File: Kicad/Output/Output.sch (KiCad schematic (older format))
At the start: 4 parts

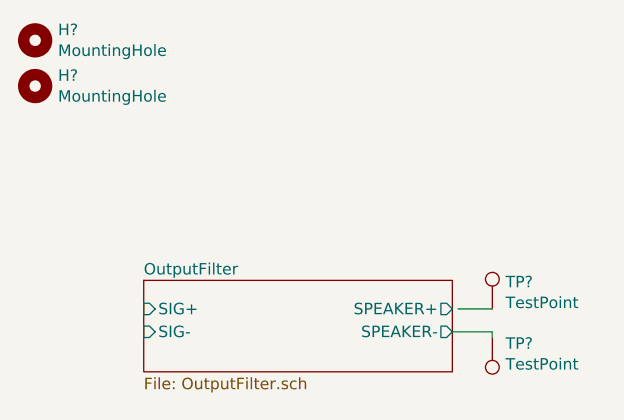
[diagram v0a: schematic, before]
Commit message: Prepared O/P Filter PCB for track layout
Laid out components for Output Filter PCB compactly ready for tracks to be drawn. Have drawn out precise margin lines too.
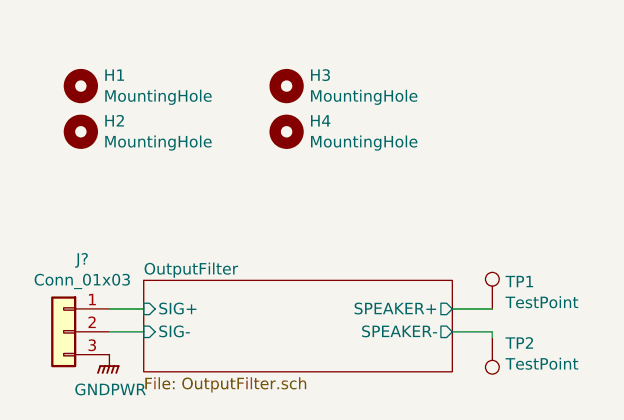
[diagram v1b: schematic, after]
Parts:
- added H3, H4: MountingHole, MountingHole:MountingHole_3.2mm_M3_ISO7380_Pad, symbol Mechanical:MountingHole
- added J?: Conn_01x03, TerminalBlock:TerminalBlock_bornier-3_P5.08mm, symbol Connector_Generic:Conn_01x03
- TP1, TP2: renamed from TP?; footprint (none) -> TestPoint:TestPoint_Pad_D2.0mm
- gave numbers to parts that had none: 2
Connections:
- net labels added: GNDPWR
- wire segments 3 -> 5
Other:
- moved on the sheet: H1, H2
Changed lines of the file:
@@
 $Descr A4 11693 8268
 encoding utf-8
-Sheet 1 1
+Sheet 1 2
 Title ""
 Date ""
@@
 $EndSheet
 $Comp
-L Connector:TestPoint TP?
+L Connector:TestPoint TP1
 U 1 1 6113ECA2
 P 4775 3000
-F 0 "TP?" H 4833 3118 50  0000 L CNN
+F 0 "TP1" H 4833 3118 50  0000 L CNN
 F 1 "TestPoint" H 4833 3027 50  0000 L CNN
-F 2 "" H 4975 3000 50  0001 C CNN
+F 2 "TestPoint:TestPoint_Pad_D2.0mm" H 4975 3000 50  0001 C CNN
 F 3 "~" H 4975 3000 50  0001 C CNN
 	1    4775 3000
@@
 $EndComp
 $Comp
-L Connector:TestPoint TP?
+L Connector:TestPoint TP2
 U 1 1 6113F2C4
 P 4775 3125
-F 0 "TP?" H 4717 3151 50  0000 R CNN
+F 0 "TP2" H 4717 3151 50  0000 R CNN
 F 1 "TestPoint" H 4717 3242 50  0000 R CNN
-F 2 "" H 4975 3125 50  0001 C CNN
+F 2 "TestPoint:TestPoint_Pad_D2.0mm" H 4975 3125 50  0001 C CNN
 F 3 "~" H 4975 3125 50  0001 C CNN
 	1    4775 3125
@@
 Wire Wire Line
 	4775 3100 4600 3100
-Wire Wire Line
-	4625 3000 4775 3000
 $Comp
-L Mechanical:MountingHole H?
+L Mechanical:MountingHole H1
 U 1 1 6113FA4B
-P 2775 1825
-F 0 "H?" H 2875 1871 50  0000 L CNN
-F 1 "MountingHole" H 2875 1780 50  0000 L CNN
-F 2 "MountingHole:MountingHole_3.2mm_M3_ISO7380_Pad" H 2775 1825 50  0001 C CNN
-F 3 "~" H 2775 1825 50  0001 C CNN
-	1    2775 1825
+P 2975 2025
+F 0 "H1" H 3075 2071 50  0000 L CNN
+F 1 "MountingHole" H 3075 1980 50  0000 L CNN
+F 2 "MountingHole:MountingHole_3.2mm_M3_ISO7380_Pad" H 2975 2025 50  0001 C CNN
+F 3 "~" H 2975 2025 50  0001 C CNN
+	1    2975 2025
 	1    0    0    -1
 $EndComp
 $Comp
-L Mechanical:MountingHole H?
+L Mechanical:MountingHole H2
 U 1 1 611402F6
-P 2775 2025
-F 0 "H?" H 2875 2071 50  0000 L CNN
-F 1 "MountingHole" H 2875 1980 50  0000 L CNN
-F 2 "MountingHole:MountingHole_3.2mm_M3_ISO7380_Pad" H 2775 2025 50  0001 C CNN
-F 3 "~" H 2775 2025 50  0001 C CNN
-	1    2775 2025
+P 2975 2225
+F 0 "H2" H 3075 2271 50  0000 L CNN
+F 1 "MountingHole" H 3075 2180 50  0000 L CNN
+F 2 "MountingHole:MountingHole_3.2mm_M3_ISO7380_Pad" H 2975 2225 50  0001 C CNN
+F 3 "~" H 2975 2225 50  0001 C CNN
+	1    2975 2225
 	1    0    0    -1
 $EndComp
+$Comp
+L Mechanical:MountingHole H3
+U 1 1 6113629F
+P 3875 2025
+F 0 "H3" H 3975 2071 50  0000 L CNN
+F 1 "MountingHole" H 3975 1980 50  0000 L CNN
+F 2 "MountingHole:MountingHole_3.2mm_M3_ISO7380_Pad" H 3875 2025 50  0001 C CNN
+F 3 "~" H 3875 2025 50  0001 C CNN
+	1    3875 2025
+	1    0    0    -1
+$EndComp
+$Comp
+L Mechanical:MountingHole H4
+U 1 1 611362A5
+P 3875 2225
+F 0 "H4" H 3975 2271 50  0000 L CNN
+F 1 "MountingHole" H 3975 2180 50  0000 L CNN
+F 2 "MountingHole:MountingHole_3.2mm_M3_ISO7380_Pad" H 3875 2225 50  0001 C CNN
+F 3 "~" H 3875 2225 50  0001 C CNN
+	1    3875 2225
+	1    0    0    -1
+$EndComp
+Wire Wire Line
+	4600 3000 4775 3000
+$Comp
+L Connector_Generic:Conn_01x03 J?
+U 1 1 61136770
+P 2900 3100
+F 0 "J?" H 2818 3417 50  0000 C CNN
+F 1 "Conn_01x03" H 2818 3326 50  0000 C CNN
+F 2 "TerminalBlock:TerminalBlock_bornier-3_P5.08mm" H 2900 3100 50  0001 C CNN
+F 3 "~" H 2900 3100 50  0001 C CNN
+	1    2900 3100
+	-1   0    0    -1
+$EndComp
+$Comp
+L power:GNDPWR #PWR?
+U 1 1 61137C19
+P 3100 3200
+F 0 "#PWR?" H 3100 3000 50  0001 C CNN
+F 1 "GNDPWR" H 3104 3046 50  0000 C CNN
+F 2 "" H 3100 3150 50  0001 C CNN
+F 3 "" H 3100 3150 50  0001 C CNN
+	1    3100 3200
+	1    0    0    -1
+$EndComp
+Wire Wire Line
+	3250 3000 3100 3000
+Wire Wire Line
+	3100 3100 3250 3100
 $EndSCHEMATC

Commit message: Update Output.sch
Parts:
- gave numbers to parts that had none: 1
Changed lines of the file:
@@
 	4600 3000 4775 3000
 $Comp
-L Connector_Generic:Conn_01x03 J?
+L Connector_Generic:Conn_01x03 J2
 U 1 1 61136770
 P 2900 3100
-F 0 "J?" H 2818 3417 50  0000 C CNN
+F 0 "J2" H 2818 3417 50  0000 C CNN
 F 1 "Conn_01x03" H 2818 3326 50  0000 C CNN
 F 2 "TerminalBlock:TerminalBlock_bornier-3_P5.08mm" H 2900 3100 50  0001 C CNN
@@
 $EndComp
 $Comp
-L power:GNDPWR #PWR?
+L power:GNDPWR #PWR0102
 U 1 1 61137C19
 P 3100 3200
-F 0 "#PWR?" H 3100 3000 50  0001 C CNN
+F 0 "#PWR0102" H 3100 3000 50  0001 C CNN
 F 1 "GNDPWR" H 3104 3046 50  0000 C CNN
 F 2 "" H 3100 3150 50  0001 C CNN
